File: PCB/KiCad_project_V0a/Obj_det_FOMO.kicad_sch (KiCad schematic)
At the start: 12 parts, among them J9 0525591853, SW1 500SSP1S2M2QEA, U2 MAX7480ESA+

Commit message: Updating Kicad files.
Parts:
- A1, A2: footprint RobotFtpLib:Nano33BLE_with_headers -> CatBot_JSC:Arduino_BLE_33; symbol RobotSymLib:Arduino_BLE_33 -> ObjDet_Library:Arduino_BLE_33
- J9: footprint RobotFtpLib:525591853 -> CON_525591853_MOL; symbol myKiCadGlobalSymbolLibrary:525591853 -> ObjDet_Library:525591853
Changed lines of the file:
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@@
 	)
 	(symbol
-		(lib_id "RobotSymLib:Arduino_BLE_33")
+		(lib_id "ObjDet_Library:Arduino_BLE_33")
 		(at 192.532 61.214 180)
 		(unit 1)
@@
 			)
 		)
-		(property "Footprint" "RobotFtpLib:Nano33BLE_with_headers"
+		(property "Footprint" "CatBot_JSC:Arduino_BLE_33"
 			(at 178.562 30.734 0)
 			(effects
@@
 			)
 		)
-		(property "Description" ""
+		(property "Description" "Arduino BLE_33"
 			(at 192.532 61.214 0)
 			(effects
@@
 	)
 	(symbol
-		(lib_id "myKiCadGlobalSymbolLibrary:525591853")
+		(lib_id "ObjDet_Library:525591853")
 		(at 249.682 40.894 0)
 		(unit 1)
@@
 			)
 		)
-		(property "Footprint" "RobotFtpLib:525591853"
-			(at 263.398 66.1669 0)
+		(property "Footprint" "CON_525591853_MOL"
+			(at 237.49 29.21 0)
 			(effects
 				(font
@@
 					(italic yes)
 				)
-				(justify left)
-				(hide yes)
-			)
-		)
-		(property "Datasheet" "559171630"
-			(at 249.682 40.894 0)
+				(hide yes)
+			)
+		)
+		(property "Datasheet" "525591853"
+			(at 242.57 36.322 0)
 			(effects
 				(font
@@
 	)
 	(symbol
-		(lib_id "RobotSymLib:Arduino_BLE_33")
+		(lib_id "ObjDet_Library:Arduino_BLE_33")
 		(at 124.46 60.706 180)
 		(unit 1)
@@
 			)
 		)
-		(property "Footprint" "RobotFtpLib:Nano33BLE_with_headers"
+		(property "Footprint" "CatBot_JSC:Arduino_BLE_33"
 			(at 110.49 30.226 0)
 			(effects
@@
 			)
 		)
-		(property "Description" ""
+		(property "Description" "Arduino BLE_33"
 			(at 124.46 60.706 0)
 			(effects

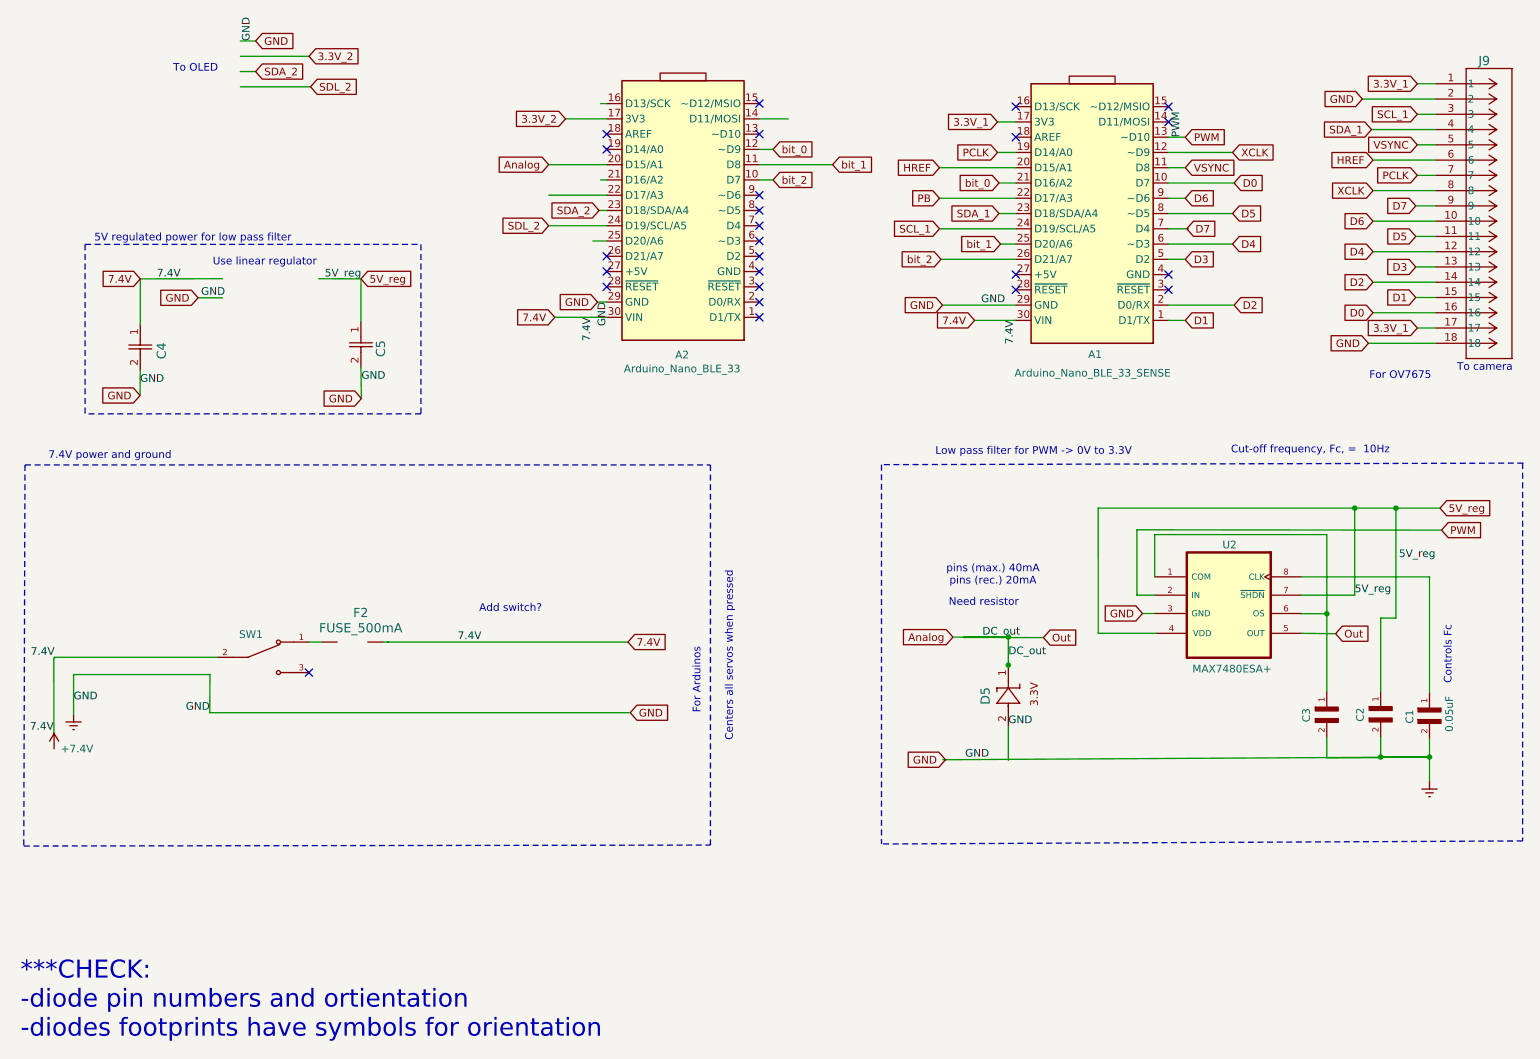
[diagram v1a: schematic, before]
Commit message: Updating PCB.
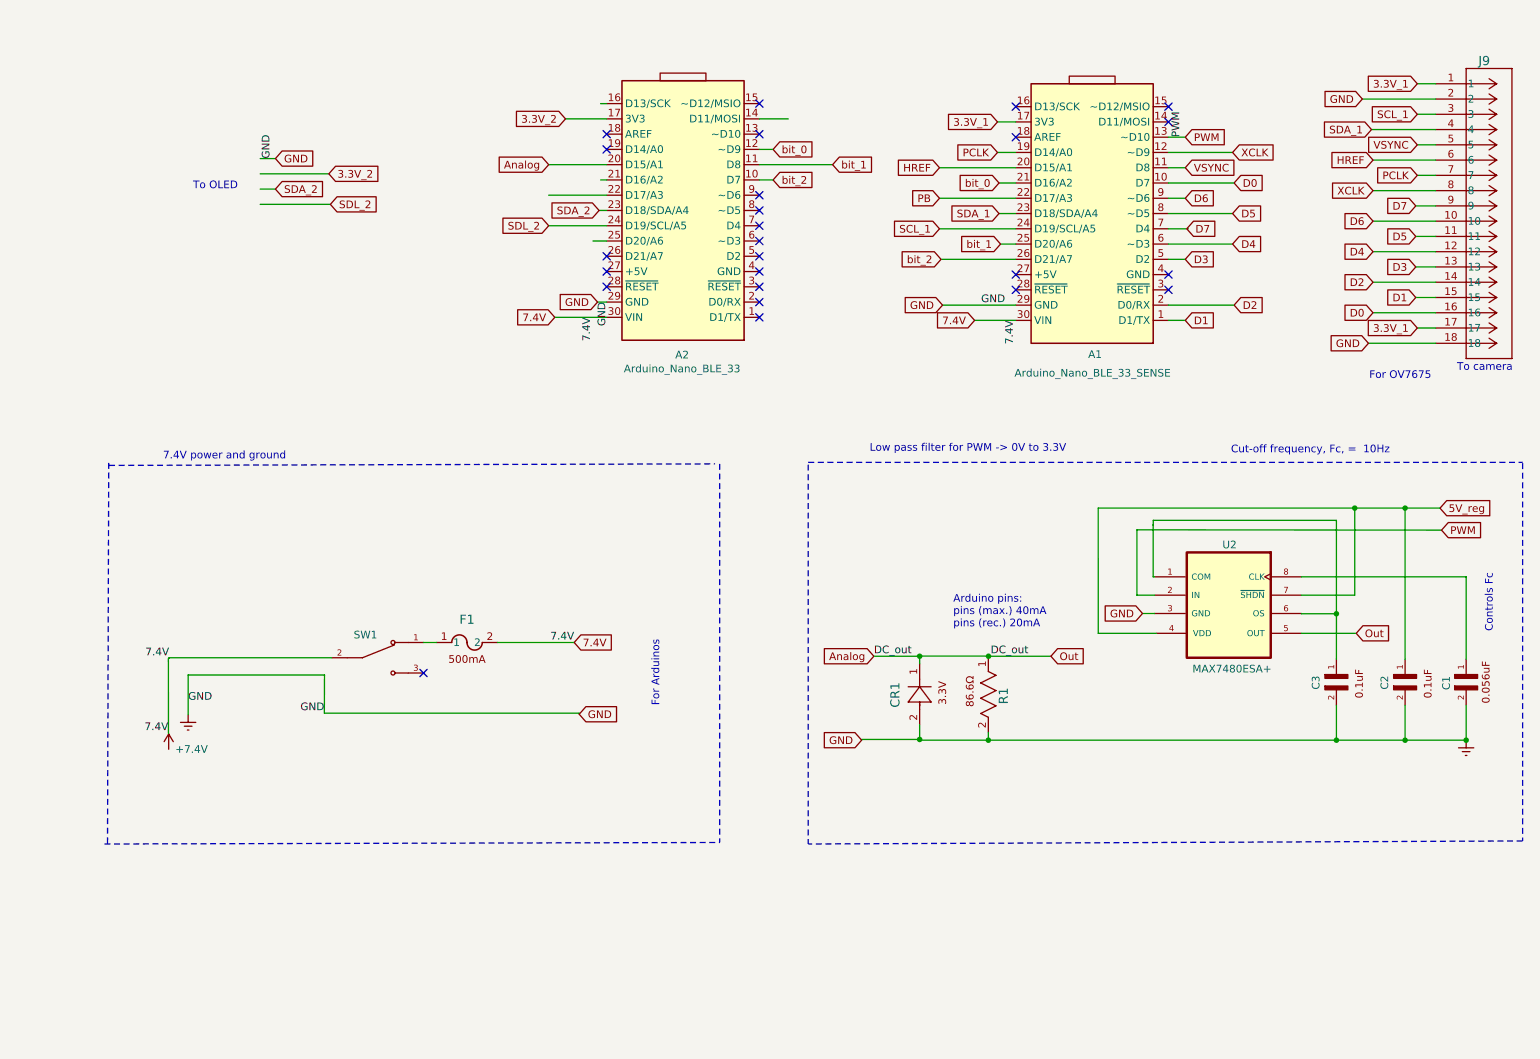
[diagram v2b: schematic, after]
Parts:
- removed C4: CL32B475KBUYNNE, RobotFtpLib:CL32B475KBUYNNE, symbol RobotSymLib:CL32B475KBUYNNE
- removed C5: CL32A106KAULNNE, RobotFtpLib:CL32A106KAULNNE, symbol RobotSymLib:CL32A106KAULNNE
- removed D5: BZT52C3V3-7-F, RobotFtpLib:BZT52C3V3-7-F, symbol RobotSymLib:BZT52C3V3-7-F
- removed F2: FUSE_500mA, RobotFtpLib:RKEF050HF, symbol RobotSymLib:RKEF050HF
- added CR1: 1N5226BFSCT-ND, symbol ObjDet_Library:1N5226BFSCT-ND
- added F1: F2339CT-ND, symbol ObjDet_Library:F2339CT-ND
- added R1: MFR-25FBF52-86R6, symbol ObjDet_Library:MFR-25FBF52-86R6
- A1, A2: footprint CatBot_JSC:Arduino_BLE_33 -> (none)
- C1: footprint RobotFtpLib:12065C503JAT2A -> (none); symbol RobotSymLib:12065C503JAT2A -> ObjDet_Library:C322C563K5R5TA
- C2, C3: footprint RobotFtpLib:12102C104KAT2A -> (none); symbol RobotSymLib:12102C104KAT2A -> ObjDet_Library:FG16C0G1H104JNT06
- U2: footprint RobotFtpLib:MAX7480ESA -> (none)
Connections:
- net 7.4V: now also F1.2
- net Analog: no longer U2.5 (OUT)
- net GNDREF: now also CR1.2, R1.2
- net at SW1.1: now also F1.1
- new net Out: CR1.1, R1.1, U2.5 (OUT)
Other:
- note added: "Arduino pins: pins (max.) 40mA pins (rec.) 20mA"
- note removed: "***CHECK: -diode pin numbers and ortientation -diodes footprints have symbols for orientation"
- note removed: "5V regulated power for low pass filter"
- note removed: "Add switch?"
- note removed: "Centers all servos when pressed"
- note removed: "Need resistor"
- note removed: "Use linear regulator"
- note removed: "pins (max.) 40mA pins (rec.) 20mA"
- moved on the sheet: SW1

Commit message: Updating KiCad.
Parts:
- added Q1: 497-1443-5-ND, symbol ObjDet_Library:497-1443-5-ND
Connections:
- net 5V_reg: now also Q1.3 (OUT)
- net 7.4V: now also Q1.1 (IN)
- net GNDREF: now also Q1.2 (GND)
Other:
- moved on the sheet: A1, A2, J9
